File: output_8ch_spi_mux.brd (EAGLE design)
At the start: 65 x 56 mm, 40 parts, among them IC1 TPS706-1V8, IC2 5M160ZE64, IC3 SN75174SOIC-20, IC4 SN75174SOIC-20, K1 PIN20X2, Q1 50MHz, U1 CAT24C256

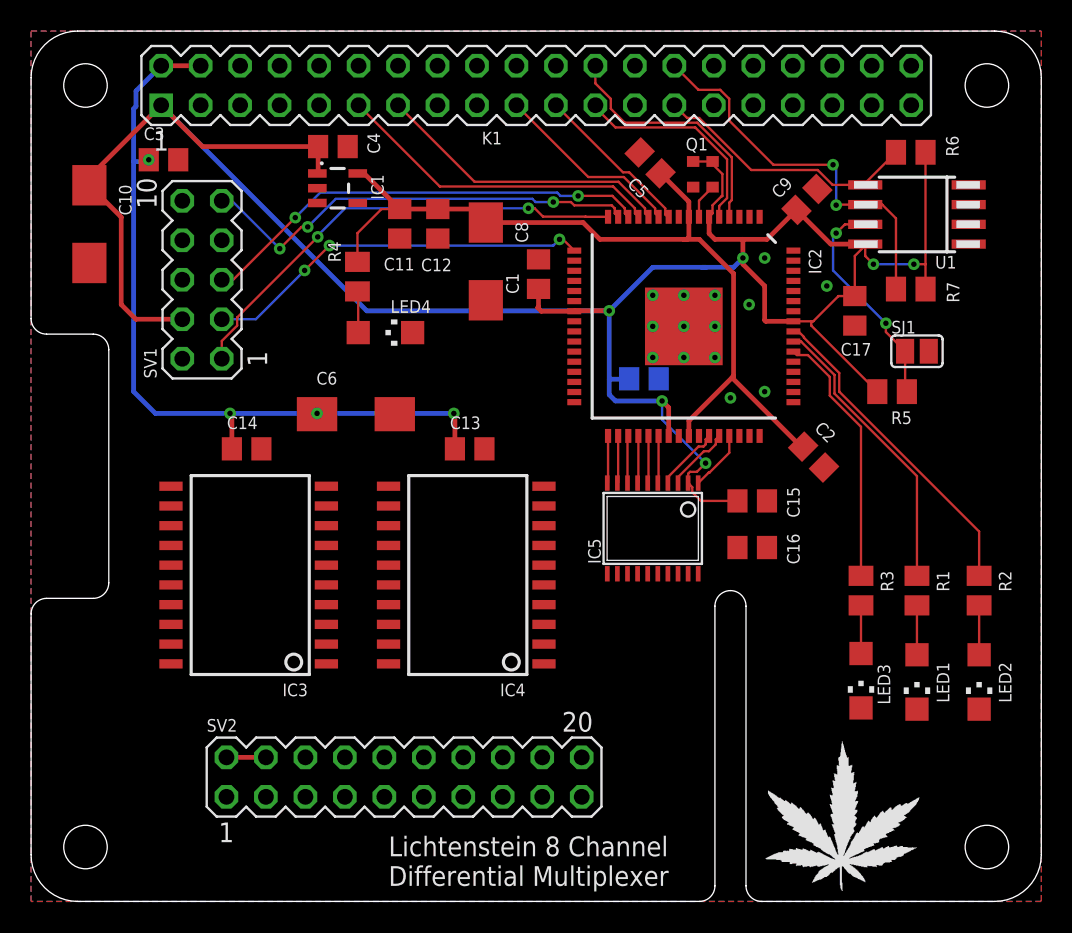
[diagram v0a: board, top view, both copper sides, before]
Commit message: finished routing differential transceivers
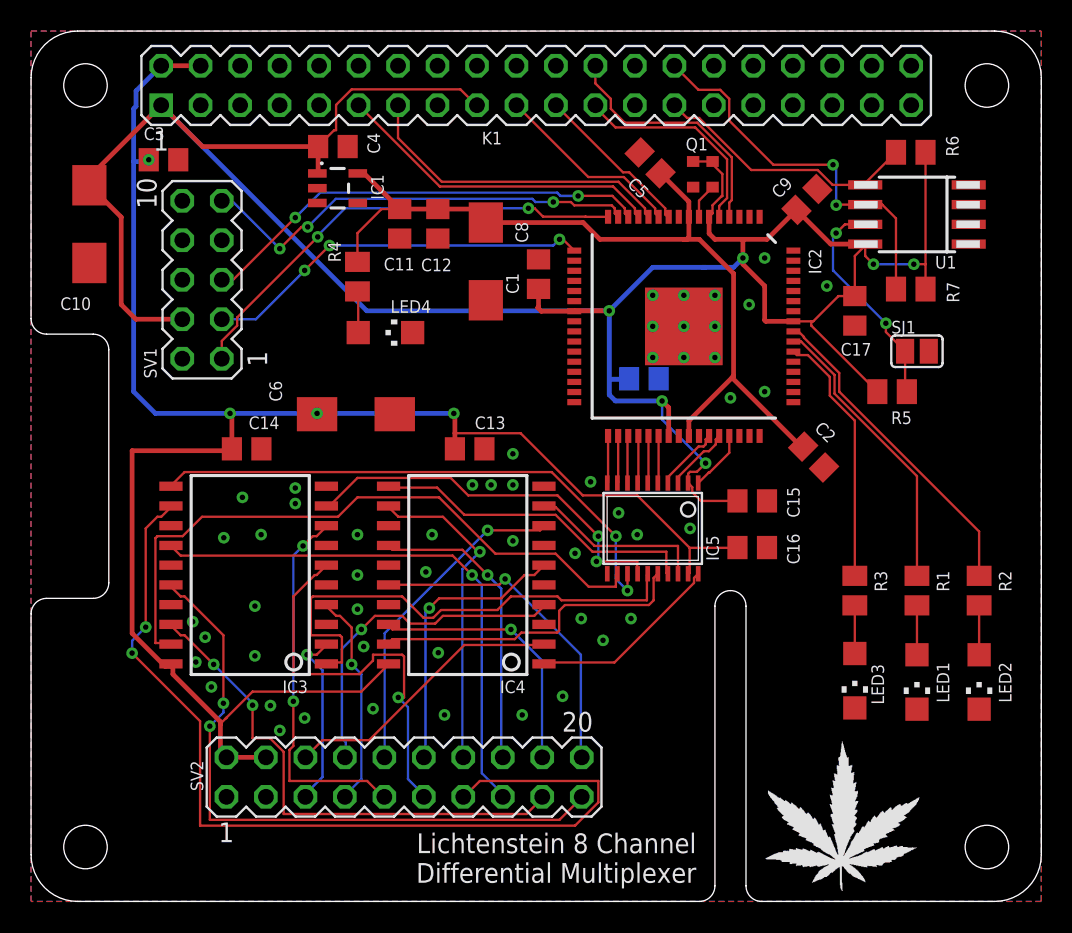
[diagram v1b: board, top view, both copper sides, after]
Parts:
- moved LED3 0.40 mm to (53.0, 14.2)
- moved R3 0.40 mm to (53.0, 20.0)
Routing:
- net +5V: track 53.7 -> 118.8 mm
- net OUT6_P: track 0.00 -> 60.3 mm, vias 0 -> 2
- net OUTPUT7: track 0.00 -> 41.8 mm
- net OUT7_N: track 0.00 -> 41.6 mm, vias 0 -> 2
- net OUTPUT6: track 0.00 -> 35.6 mm, vias 0 -> 2
- net OUT6_N: track 0.00 -> 35.3 mm, vias 0 -> 1
- net OUT7_P: track 0.00 -> 33.2 mm, vias 0 -> 2
- net OUTPUT4: track 0.00 -> 31.8 mm
- net OUT5_N: track 0.00 -> 26.0 mm, vias 0 -> 1
- net OUTPUT5: track 0.00 -> 24.9 mm, vias 0 -> 2
- net OUT5_P: track 0.00 -> 24.1 mm, vias 0 -> 2
- net OUT0_N: track 0.00 -> 21.7 mm, vias 0 -> 1
- net OUT3_N: track 0.00 -> 21.2 mm, vias 0 -> 1
- net OUTPUT2: track 0.00 -> 21.2 mm
- net OUT1_P: track 0.00 -> 21.1 mm, vias 0 -> 1
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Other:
- board text added: "VCORE Good"

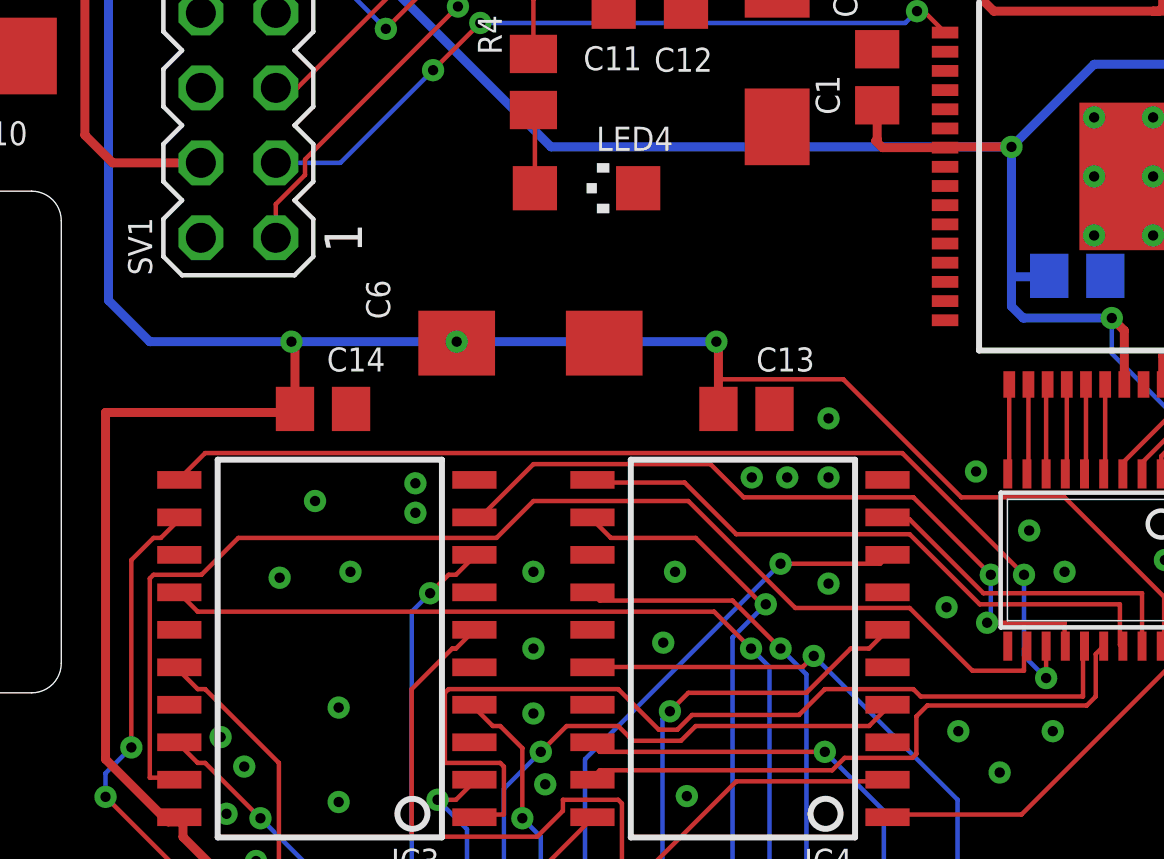
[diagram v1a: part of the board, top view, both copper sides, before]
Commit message: routed missing differential driver enables
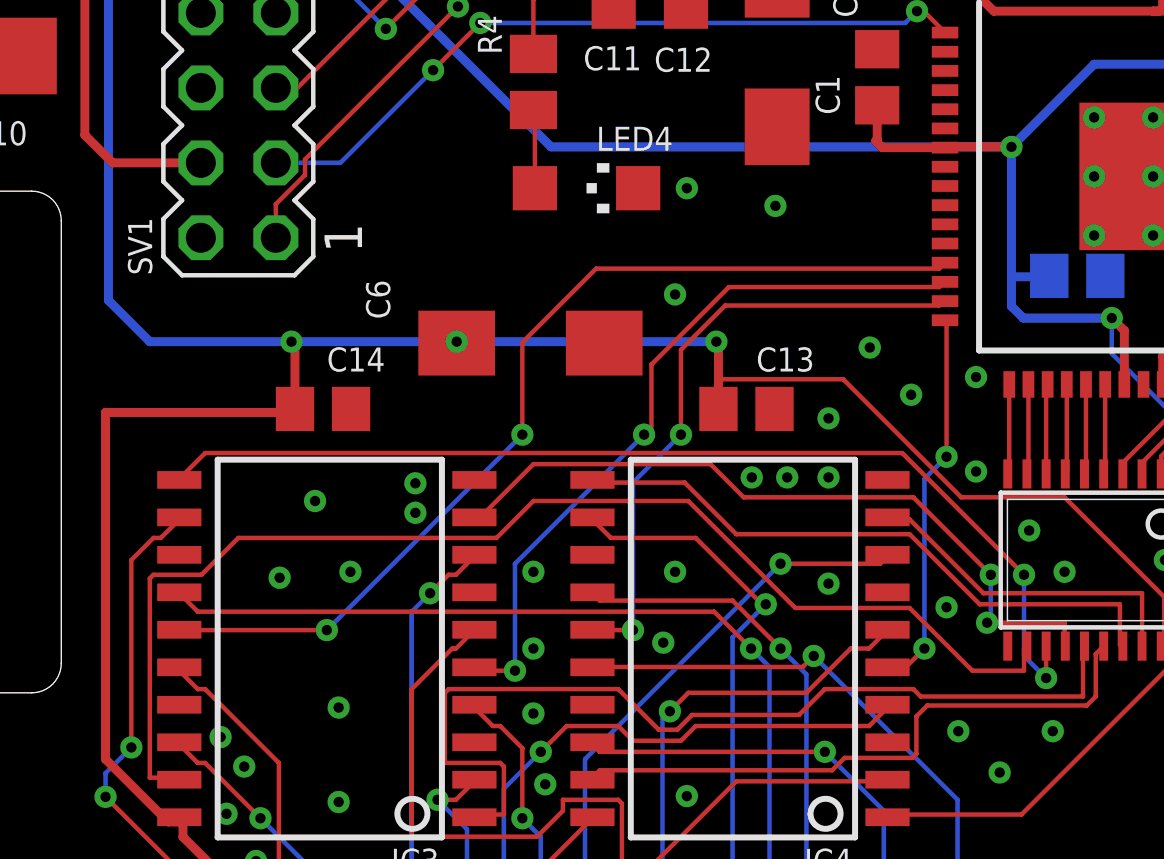
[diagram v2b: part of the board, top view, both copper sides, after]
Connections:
- removed net OUT01_OE: IC2.32
- removed net OUT23_OE: IC2.31
- removed net OUT45_OE: IC2.30
- removed net OUT67_OE: IC2.29
- net OUT01_EN: now also IC2.32
- net OUT23_EN: now also IC2.31
- net OUT45_EN: now also IC2.30
- net OUT67_EN: now also IC2.29
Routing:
- net OUT67_EN: track 0.00 -> 32.9 mm, vias 0 -> 2
- net OUT45_EN: track 0.00 -> 25.0 mm, vias 0 -> 2
- net OUT23_EN: track 0.00 -> 21.2 mm, vias 0 -> 2
- net OUT01_EN: track 0.00 -> 13.0 mm, vias 0 -> 2
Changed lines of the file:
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@@
 <via x="17" y="25.6" extent="1-16" drill="0.35"/>
 <via x="36.8" y="16.8" extent="1-16" drill="0.35"/>
+<via x="33.8" y="29.6" extent="1-16" drill="0.35"/>
+<via x="32.4" y="31.2" extent="1-16" drill="0.35"/>
+<via x="36" y="30.2" extent="1-16" drill="0.35"/>
+<via x="29.2" y="36" extent="1-16" drill="0.35"/>
+<via x="26.2" y="36.6" extent="1-16" drill="0.35"/>
+<via x="25.8" y="33" extent="1-16" drill="0.35"/>
 </signal>
 <signal name="CPLD_TMS">
@@
 <signal name="OUT67_EN">
 <contactref element="IC3" pad="15"/>
+<contactref element="IC2" pad="29"/>
+<wire x1="34.75" y1="33.875" x2="34.875" y2="34" width="0.1524" layer="1"/>
+<wire x1="23.125" y1="33.875" x2="34.75" y2="33.875" width="0.1524" layer="1"/>
+<wire x1="20.625" y1="31.375" x2="23.125" y2="33.875" width="0.1524" layer="1"/>
+<wire x1="20.625" y1="28.25" x2="20.625" y2="31.375" width="0.1524" layer="1"/>
+<wire x1="14" y1="21.625" x2="20.625" y2="28.25" width="0.1524" layer="16"/>
+<wire x1="9" y1="21.625" x2="14" y2="21.625" width="0.1524" layer="1"/>
+<wire x1="34.875" y1="34" x2="34.95" y2="34.075" width="0.1524" layer="1"/>
+<wire x1="9" y1="21.625" x2="9" y2="21.635" width="0.1524" layer="1"/>
+<via x="20.625" y="28.25" extent="1-16" drill="0.35"/>
+<via x="14" y="21.625" extent="1-16" drill="0.35"/>
 </signal>
 <signal name="OUT45_EN">
 <contactref element="IC3" pad="5"/>
+<contactref element="IC2" pad="30"/>
+<wire x1="34.75" y1="33.25" x2="34.875" y2="33.375" width="0.1524" layer="1"/>
+<wire x1="27.625" y1="33.25" x2="34.75" y2="33.25" width="0.1524" layer="1"/>
+<wire x1="25" y1="30.625" x2="27.625" y2="33.25" width="0.1524" layer="1"/>
+<wire x1="25" y1="28.25" x2="25" y2="30.625" width="0.1524" layer="1"/>
+<wire x1="24.75" y1="28.25" x2="25" y2="28.25" width="0.1524" layer="1"/>
+<wire x1="20.375" y1="23.875" x2="24.75" y2="28.25" width="0.1524" layer="16"/>
+<wire x1="20.375" y1="20.25" x2="20.375" y2="23.875" width="0.1524" layer="16"/>
+<wire x1="19" y1="20.25" x2="20.375" y2="20.25" width="0.1524" layer="1"/>
+<wire x1="34.875" y1="33.375" x2="34.95" y2="33.425" width="0.1524" layer="1"/>
+<wire x1="19" y1="20.25" x2="19" y2="20.365" width="0.1524" layer="1"/>
+<via x="24.75" y="28.25" extent="1-16" drill="0.35"/>
+<via x="20.375" y="20.25" extent="1-16" drill="0.35"/>
 </signal>
 <signal name="OUT23_EN">
 <contactref element="IC4" pad="15"/>
+<contactref element="IC2" pad="31"/>
+<wire x1="34.75" y1="32.625" x2="34.875" y2="32.75" width="0.1524" layer="1"/>
+<wire x1="27.5" y1="32.625" x2="34.75" y2="32.625" width="0.1524" layer="1"/>
+<wire x1="26" y1="31.125" x2="27.5" y2="32.625" width="0.1524" layer="1"/>
+<wire x1="26" y1="28.25" x2="26" y2="31.125" width="0.1524" layer="1"/>
+<wire x1="24.375" y1="26.625" x2="26" y2="28.25" width="0.1524" layer="16"/>
+<wire x1="24.375" y1="21.625" x2="24.375" y2="26.625" width="0.1524" layer="16"/>
+<wire x1="23" y1="21.625" x2="24.375" y2="21.625" width="0.1524" layer="1"/>
+<wire x1="34.875" y1="32.75" x2="34.95" y2="32.775" width="0.1524" layer="1"/>
+<wire x1="23" y1="21.625" x2="23" y2="21.635" width="0.1524" layer="1"/>
+<via x="26" y="28.25" extent="1-16" drill="0.35"/>
+<via x="24.375" y="21.625" extent="1-16" drill="0.35"/>
 </signal>
 <signal name="OUT01_EN">
 <contactref element="IC4" pad="5"/>
+<contactref element="IC2" pad="32"/>
+<wire x1="35" y1="27.5" x2="35" y2="32.125" width="0.1524" layer="1"/>
+<wire x1="34.25" y1="26.75" x2="35" y2="27.5" width="0.1524" layer="16"/>
+<wire x1="34.25" y1="21" x2="34.25" y2="26.75" width="0.1524" layer="16"/>
+<wire x1="33.625" y1="20.375" x2="34.25" y2="21" width="0.1524" layer="1"/>
+<wire x1="33" y1="20.375" x2="33.625" y2="20.375" width="0.1524" layer="1"/>
+<wire x1="35" y1="32.125" x2="34.95" y2="32.125" width="0.1524" layer="1"/>
+<wire x1="33" y1="20.375" x2="33" y2="20.365" width="0.1524" layer="1"/>
+<via x="35" y="27.5" extent="1-16" drill="0.35"/>
+<via x="34.25" y="21" extent="1-16" drill="0.35"/>
 </signal>
 <signal name="N$3">
@@
 <wire x1="46.335103125" y1="47.060296875" x2="50.61573125" y2="47.060296875" width="0.1524" layer="1"/>
 </signal>
-<signal name="OUT01_OE">
-<contactref element="IC2" pad="32"/>
-</signal>
-<signal name="OUT23_OE">
-<contactref element="IC2" pad="31"/>
-</signal>
-<signal name="OUT45_OE">
-<contactref element="IC2" pad="30"/>
-</signal>
-<signal name="OUT67_OE">
-<contactref element="IC2" pad="29"/>
-</signal>
 <signal name="N$2">

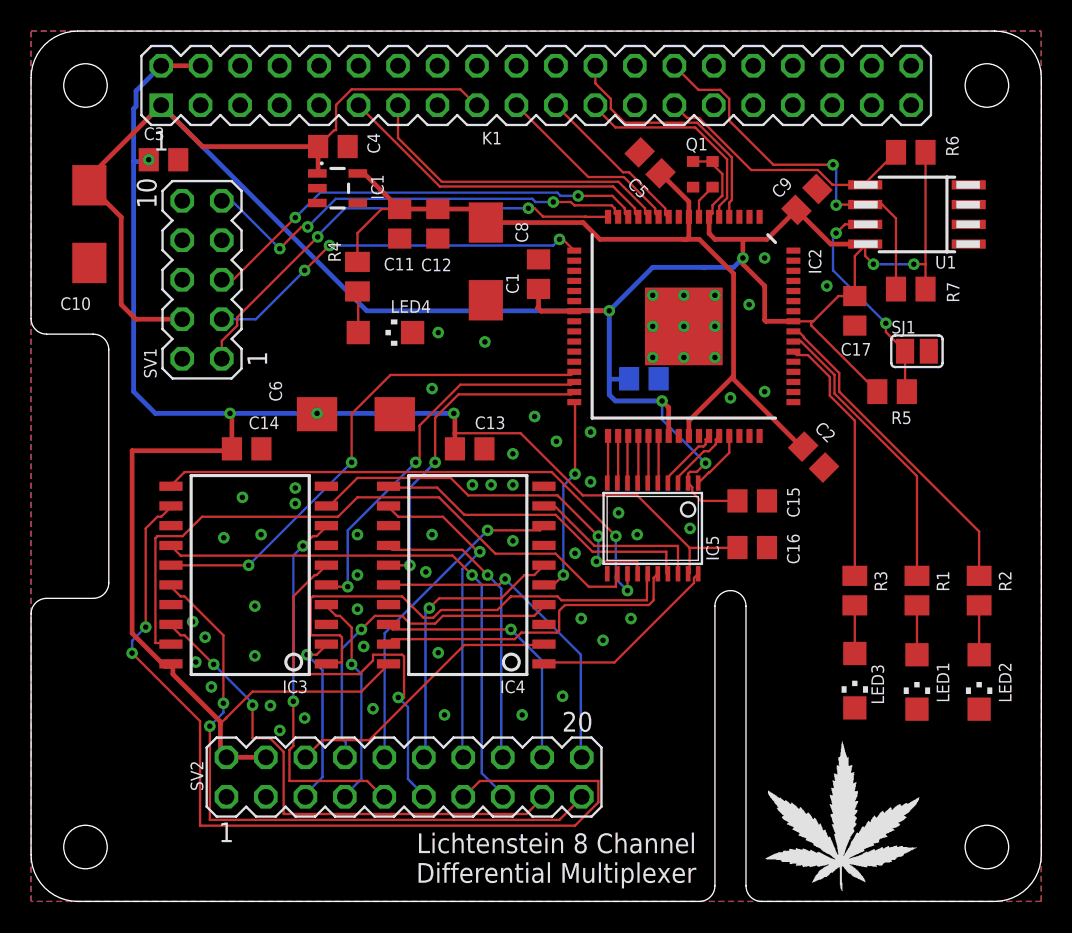
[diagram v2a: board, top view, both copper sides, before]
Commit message: Added MCP2517FD CAN transceiver
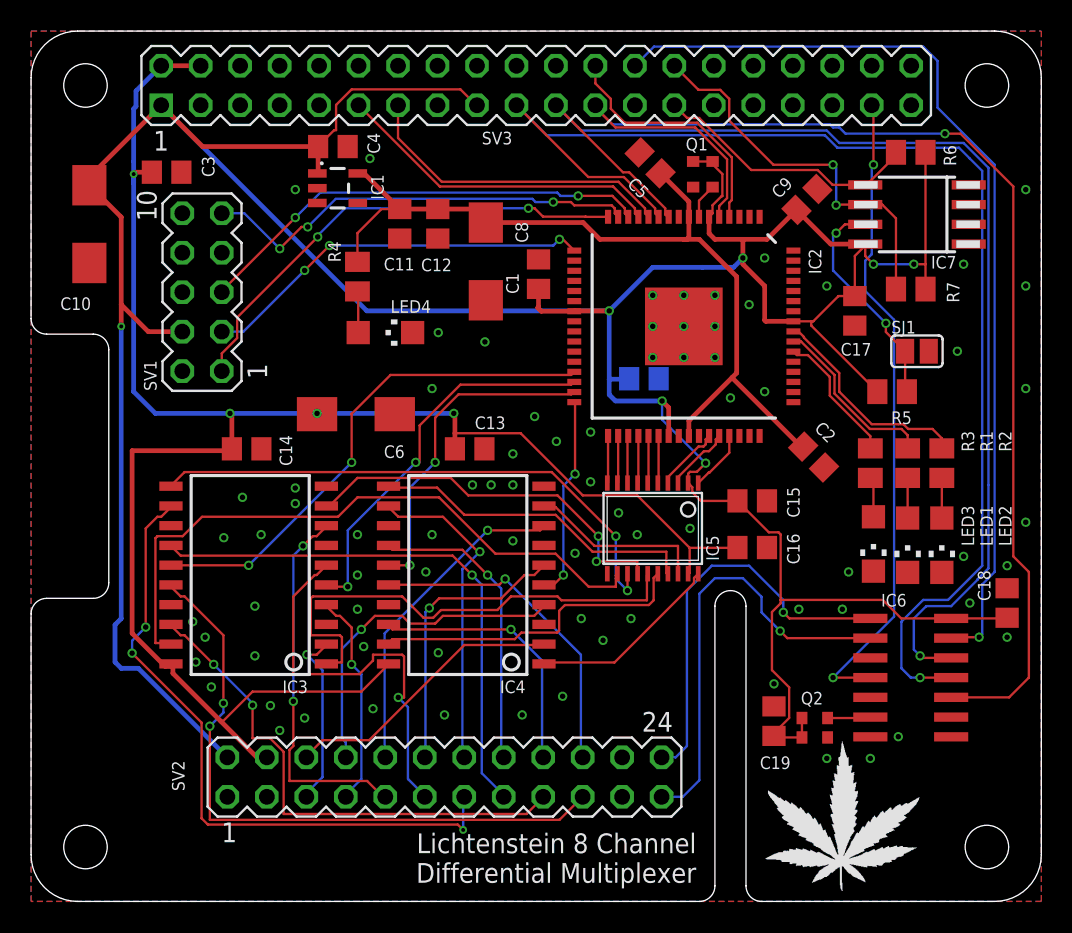
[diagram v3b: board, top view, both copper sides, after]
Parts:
- added C18, C19: 100nF, rcl:C0805
- added IC6: MCP2517FDSOIC-14, lichtenstein_onion:SO-14
- added Q2: 20MHz, lichtenstein_onion:VLGA-4
- SV2: device con-lstb:MA10-2 -> con-lstb:MA12-2
- moved LED2 9.12 mm to (58.6, 22.9)
- moved LED3 8.88 mm to (54.2, 23.0)
- moved LED1 8.82 mm to (56.4, 22.9)
- moved R2 8.54 mm to (58.6, 28.2)
- moved R3 8.26 mm to (54.0, 28.2)
- moved R1 8.22 mm to (56.4, 28.2)
- moved SV2 2.60 mm to (26.6, 8.00)
- moved C3 0.82 mm to (8.72, 46.9)
- moved SV1 0.80 mm to (11.0, 39.2)
- renumbered K1 to SV3, U1 to IC7
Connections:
- net !SPI_CS renamed !SPI_CS0
- new net !CAN_INT: IC6.4, SV3.37
- new net !SPI_CS1: IC6.13, SV3.26
- new net CAN_RX: IC6.2, SV2.23
- new net CAN_TX: IC6.1, SV2.24
- new net CLK_20: IC6.6, Q2.3
- net +3V3: now also C18.1, C19.1, IC6.14, Q2.1, Q2.4, SV2.2
- net +5V: no longer SV2.2
- net GND: now also C18.2, C19.2, IC6.7, Q2.2, SV2.21, SV2.22
- net SPI_MISO: now also IC6.12
- net SPI_MOSI: now also IC6.11
- net SPI_SCK: now also IC6.10
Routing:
- net SPI_MOSI: track 12.3 -> 82.6 mm, vias 0 -> 1
- net +3V3: track 174.5 -> 243.5 mm, vias 6 -> 7
- net SPI_SCK: track 13.9 -> 80.6 mm, vias 0 -> 1
- net SPI_MISO: track 10.5 -> 76.5 mm, vias 0 -> 1
- net !SPI_CS1: track 0.00 -> 61.2 mm, vias 0 -> 1
- net !CAN_INT: track 0.00 -> 41.9 mm, vias 0 -> 2
- net CAN_RX: track 0.00 -> 28.5 mm, vias 0 -> 1
- net CAN_TX: track 0.00 -> 26.3 mm, vias 0 -> 1
- net OUT6_P: track 60.3 -> 42.4 mm, vias 2 -> 3
- net STATUS2: track 16.5 -> 8.69 mm
- net STATUS0: track 18.7 -> 11.4 mm
- net STATUS1: track 20.9 -> 13.8 mm
- net CLK_20: track 0.00 -> 2.77 mm
- net +5V: track 118.8 -> 118.0 mm
- net CPLD_TCK: track 30.2 -> 31.0 mm
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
